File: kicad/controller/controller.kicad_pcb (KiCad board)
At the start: 2 copper layers, 52 x 29 mm, 40 parts, among them J1 JST_BAT, J2 JST_BOOKMARK, J3 CONN_UPDI, J4 UART_DBG, Q1 DMP1045U, SW1 SW_DIP_x01, U1 DS3231, U2 TP4056, U3 ATTINY1616

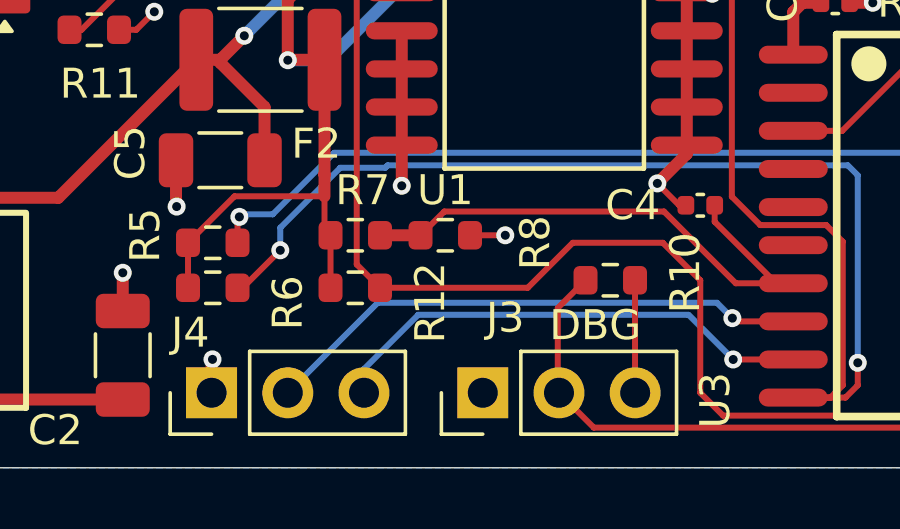
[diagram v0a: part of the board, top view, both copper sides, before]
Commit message: fix: fix wrong UPDI & DBG pin label
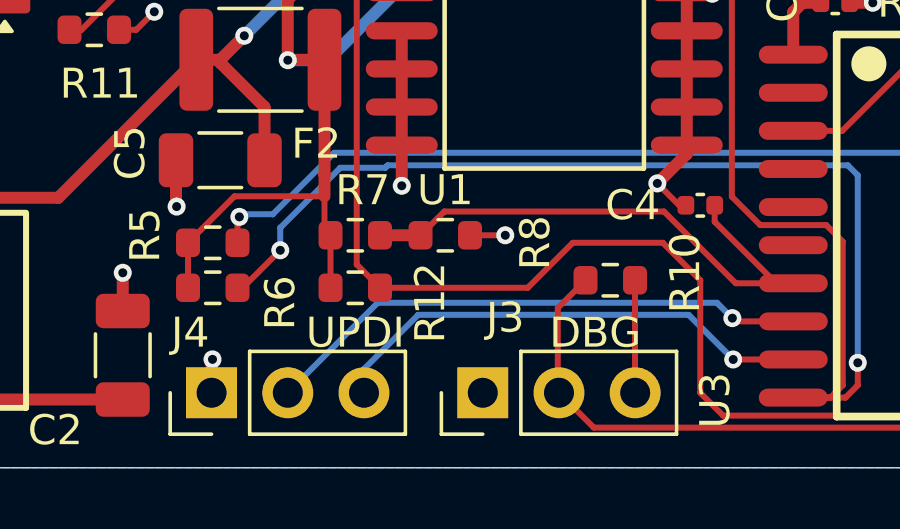
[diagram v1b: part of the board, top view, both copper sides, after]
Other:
- board text added: "UPDI"

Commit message: fix: make sense of the connection from power to peripherals make the DS3231 get power directly without a switch and add testing pads to connect power to MCU & LEDs in order to measure current.
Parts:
- added H1: VIN_DBG, Connector_Wire:SolderWirePad_1x01_SMD_1x2mm, F.Cu at (21.0, 32.3)
- added H2: PERPH_VIN_DBG, Connector_Wire:SolderWirePad_1x01_SMD_1x2mm, F.Cu at (18.4, 42.2)
- moved F2 20.3 mm to (17.5, 34.5), turned to -90 degrees
- moved C2 10.4 mm to (35.5, 30.2), turned to -90 degrees
- moved SW1 4.06 mm to (21.0, 38.3)
- moved J1 2.22 mm to (28.0, 39.0)
- moved C5 0.50 mm to (36.5, 33.8)
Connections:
- C3 pad 1: Net-(J2-VIN) -> Net-(U1A-VCC)
- C5 pad 1: Net-(C5-Pad1) -> Net-(U1A-VCC)
- F2 pad 1: Net-(C5-Pad1) -> Net-(D5-K)
- F2 pad 2: Net-(J2-VIN) -> Net-(U1A-VCC)
- R1 pad 1: Net-(C5-Pad1) -> Net-(U1A-VCC)
- SW1 pad 1: Net-(D5-K) -> Net-(U1A-VCC)
- SW1 pad 2: Net-(C5-Pad1) -> Net-(J2-VIN)
- U1 pad 2: Net-(J2-VIN) -> Net-(U1A-VCC)
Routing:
- net Net-(U1A-VCC): track 0.00 -> 57.3 mm
- net Net-(C5-Pad1): track 39.3 -> 0.00 mm, vias 2 -> 0
- net Net-(J1-VCC): track 53.7 -> 31.5 mm
- net Net-(J2-VIN): track 70.0 -> 60.1 mm
- net GND: track 37.7 -> 38.3 mm
